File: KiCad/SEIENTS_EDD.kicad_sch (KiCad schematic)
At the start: 0 parts

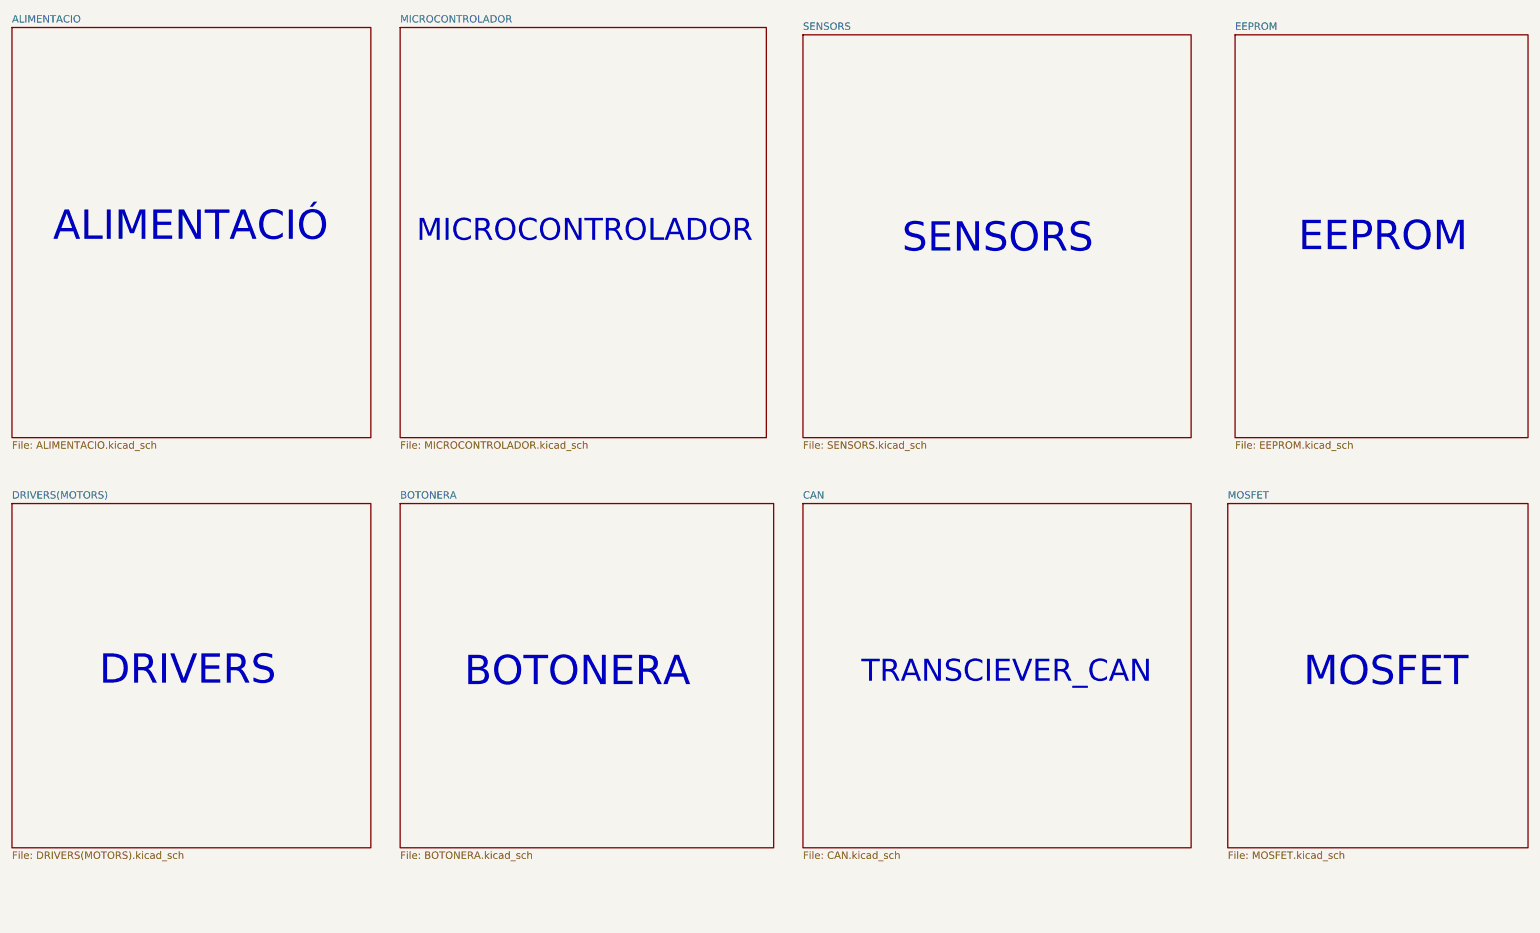
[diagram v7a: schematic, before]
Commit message: Arreglada la EEPROM
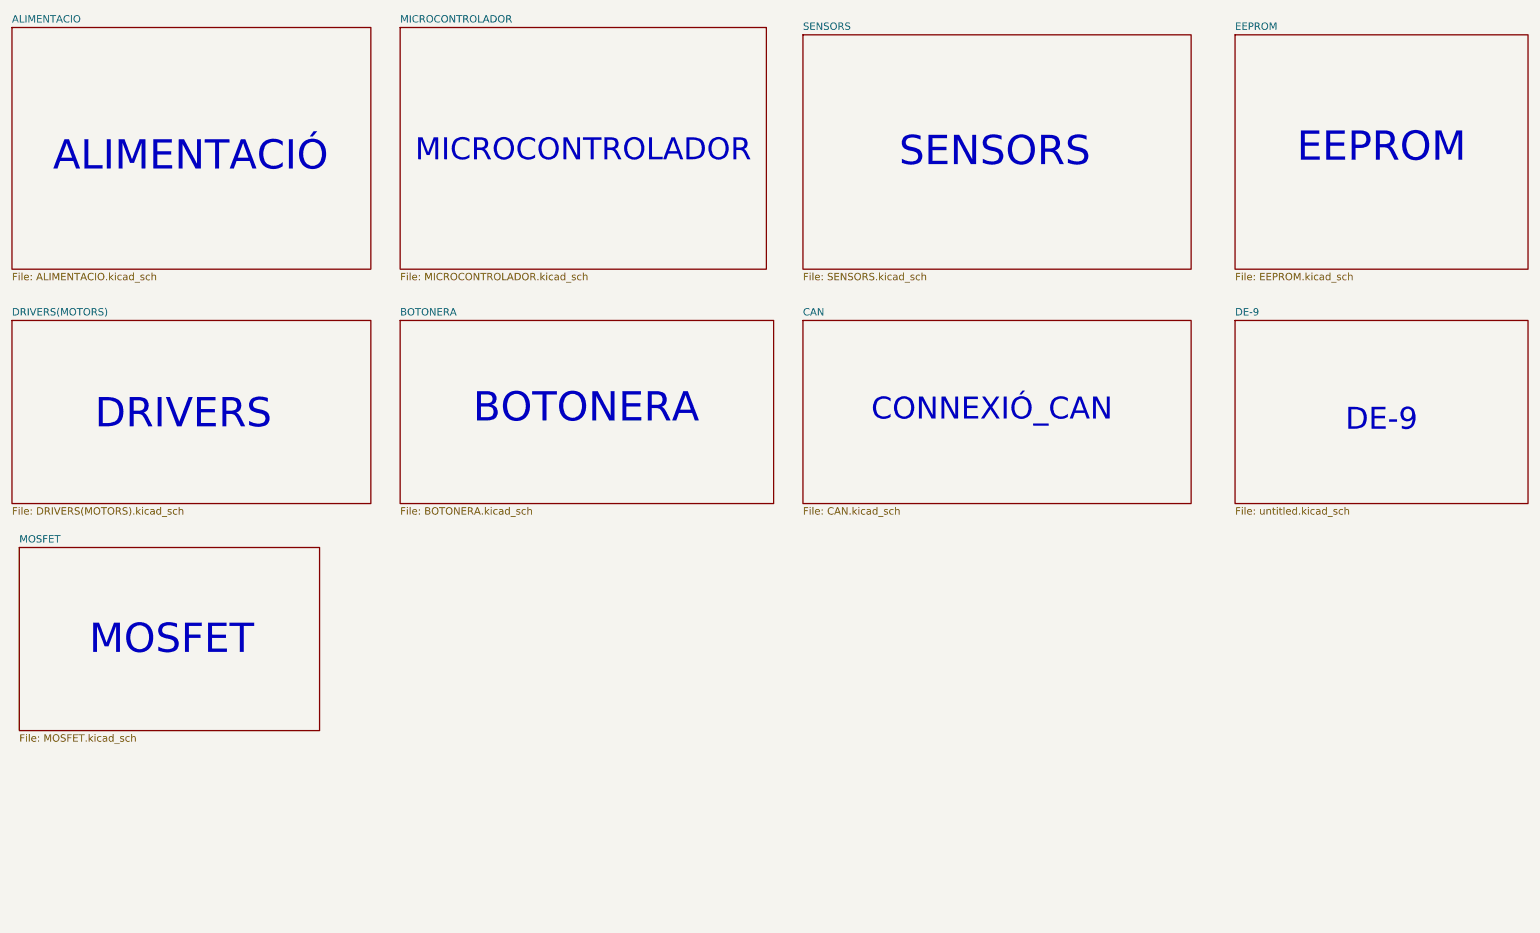
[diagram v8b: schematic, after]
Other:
- added sheet DE-9 (untitled.kicad_sch)
- note added: "CONNEXIÓ_CAN"
- note added: "DE-9"
- note removed: "TRANSCIEVER_CAN"
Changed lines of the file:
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@@
 	(generator_version "9.0")
 	(paper "A4")
-	(text "TRANSCIEVER_CAN"
-		(exclude_from_sim no)
-		(at 188.976 129.54 0)
+	(text "CONNEXIÓ_CAN"
+		(exclude_from_sim no)
+		(at 186.436 84.074 0)
 		(effects
 			(font
@@
 	(text "DRIVERS"
 		(exclude_from_sim no)
-		(at 46.99 129.286 0)
-		(effects
-			(font
-				(size 5.08 5.08)
+		(at 46.228 84.836 0)
+		(effects
+			(font
+				(size 5.08 5.08)
+			)
+		)
+	)
+	(text "DE-9"
+		(exclude_from_sim no)
+		(at 254 85.852 0)
+		(effects
+			(font
+				(size 3.81 3.81)
 			)
 		)
@@
 	(text "SENSORS"
 		(exclude_from_sim no)
-		(at 187.452 54.356 0)
+		(at 186.944 39.37 0)
 		(effects
 			(font
@@
 	(text "ALIMENTACIÓ"
 		(exclude_from_sim no)
-		(at 47.498 52.324 0)
+		(at 47.498 40.132 0)
 		(effects
 			(font
@@
 	(text "EEPROM"
 		(exclude_from_sim no)
-		(at 254.254 54.102 0)
+		(at 254 38.608 0)
 		(effects
 			(font
@@
 	(text "MICROCONTROLADOR\n"
 		(exclude_from_sim no)
-		(at 115.824 53.086 0)
+		(at 115.57 39.116 0)
 		(effects
 			(font
@@
 	(text "MOSFET\n"
 		(exclude_from_sim no)
-		(at 254.762 129.54 0)
+		(at 44.196 123.952 0)
 		(effects
 			(font
@@
 	(text "BOTONERA"
 		(exclude_from_sim no)
-		(at 114.554 129.54 0)
-		(effects
-			(font
-				(size 5.08 5.08)
-			)
-		)
-	)
-	(sheet
-		(at 153.67 100.33)
-		(size 67.31 59.69)
+		(at 116.078 83.82 0)
+		(effects
+			(font
+				(size 5.08 5.08)
+			)
+		)
+	)
+	(sheet
+		(at 153.67 68.58)
+		(size 67.31 31.75)
 		(exclude_from_sim no)
 		(in_bom yes)
@@
 		)
 		(property "Sheetname" "CAN"
-			(at 153.67 99.6184 0)
+			(at 153.67 67.8684 0)
 			(effects
 				(font
@@
 		)
 		(property "Sheetfile" "CAN.kicad_sch"
-			(at 153.67 160.6046 0)
+			(at 153.67 100.9146 0)
 			(effects
 				(font
@@
 	(sheet
 		(at 83.82 17.78)
-		(size 63.5 71.12)
+		(size 63.5 41.91)
 		(exclude_from_sim no)
 		(in_bom yes)
@@
 		)
 		(property "Sheetfile" "MICROCONTROLADOR.kicad_sch"
-			(at 83.82 89.4846 0)
+			(at 83.82 60.2746 0)
 			(effects
 				(font
@@
 	)
 	(sheet
+		(at 228.6 68.58)
+		(size 50.8 31.75)
+		(exclude_from_sim no)
+		(in_bom yes)
+		(on_board yes)
+		(dnp no)
+		(fields_autoplaced yes)
+		(stroke
+			(width 0.1524)
+			(type solid)
+		)
+		(fill
+			(color 0 0 0 0.0000)
+		)
+		(property "Sheetname" "DE-9"
+			(at 228.6 67.8684 0)
+			(effects
+				(font
+					(size 1.27 1.27)
+				)
+				(justify left bottom)
+			)
+		)
+		(property "Sheetfile" "untitled.kicad_sch"
+			(at 228.6 100.9146 0)
+			(effects
+				(font
+					(size 1.27 1.27)
+				)
+				(justify left top)
+			)
+		)
+		(instances
+			(project "SEIENTS_EDD"
+				(path "/b6401b4f-5426-49b8-bb2e-8ecdb19989ef"
+					(page "10")
+				)
+			)
+		)
+	)
+	(sheet
 		(at 16.51 17.78)
-		(size 62.23 71.12)
+		(size 62.23 41.91)
 		(exclude_from_sim no)
 		(in_bom yes)
@@
 		)
 		(property "Sheetfile" "ALIMENTACIO.kicad_sch"
-			(at 16.51 89.4846 0)
+			(at 16.51 60.2746 0)
 			(effects
 				(font
@@
 	)
 	(sheet
-		(at 16.51 100.33)
-		(size 62.23 59.69)
+		(at 16.51 68.58)
+		(size 62.23 31.75)
 		(exclude_from_sim no)
 		(in_bom yes)
@@
 		)
 		(property "Sheetname" "DRIVERS(MOTORS)"
-			(at 16.51 99.6184 0)
+			(at 16.51 67.8684 0)
 			(effects
 				(font
@@
 		)
 		(property "Sheetfile" "DRIVERS(MOTORS).kicad_sch"
-			(at 16.51 160.6046 0)
+			(at 16.51 100.9146 0)
 			(effects
 				(font
@@
 	)
 	(sheet
-		(at 83.82 100.33)
-		(size 64.77 59.69)
+		(at 83.82 68.58)
+		(size 64.77 31.75)
 		(exclude_from_sim no)
 		(in_bom yes)
@@
 		)
 		(property "Sheetname" "BOTONERA"
-			(at 83.82 99.6184 0)
+			(at 83.82 67.8684 0)
 			(effects
 				(font
@@
 		)
 		(property "Sheetfile" "BOTONERA.kicad_sch"
-			(at 83.82 160.6046 0)
+			(at 83.82 100.9146 0)
 			(effects
 				(font
@@
 	)
 	(sheet
-		(at 227.33 100.33)
-		(size 52.07 59.69)
+		(at 17.78 107.95)
+		(size 52.07 31.75)
 		(exclude_from_sim no)
 		(in_bom yes)
@@
 		)
 		(property "Sheetname" "MOSFET"
-			(at 227.33 99.6184 0)
+			(at 17.78 107.2384 0)
 			(effects
 				(font
@@
 		)
 		(property "Sheetfile" "MOSFET.kicad_sch"
-			(at 227.33 160.6046 0)
+			(at 17.78 140.2846 0)
 			(effects
 				(font
@@
 	(sheet
 		(at 228.6 19.05)
-		(size 50.8 69.85)
+		(size 50.8 40.64)
 		(exclude_from_sim no)
 		(in_bom yes)
@@
 		)
 		(property "Sheetfile" "EEPROM.kicad_sch"
-			(at 228.6 89.4846 0)
+			(at 228.6 60.2746 0)
 			(effects
 				(font
@@
 	(sheet
 		(at 153.67 19.05)
-		(size 67.31 69.85)
+		(size 67.31 40.64)
 		(exclude_from_sim no)
 		(in_bom yes)
@@
 		)
 		(property "Sheetfile" "SENSORS.kicad_sch"
-			(at 153.67 89.4846 0)
-			(effects
-				(font
+			(at 153.67 60.2746 0)
+			(effects
+				(font
